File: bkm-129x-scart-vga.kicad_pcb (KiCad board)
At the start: 2 copper layers, 105 x 160 mm, 64 parts, among them J1 DB15_Female_HighDensity_Mount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, J2 SCART-F, J3 SJ1-353XNG, J5 Conn_02x32_Row_Letter_Last, J6 ICSP, Q1 DTC144EKA, Q2 MMBT3904, SW1 PBH4UEENAGX, SW2 PBH4UEENAGX, U1 ADG1611, U2 THS7374, U3 arduino-nano-v3, U4 74LVC125, U5 MIC3490-3.3, U6 ATMEGA328PB-AU, Y1 CSTNE16M0VH3L000R0

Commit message: Rev. C. Move to Kicad 5
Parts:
- moved R16 14.6 mm to (56.4, 48.5)
- moved D2 11.5 mm to (51.6, 48.5)
- moved SW1 6.59 mm to (62.3, 41.4)
- moved Q2 3.56 mm to (69.8, 32.0)
- moved R14 3.56 mm to (62.7, 35.0)
- moved R3 3.56 mm to (69.5, 34.9)
- moved R4 3.56 mm to (75.3, 32.9)
- moved R5 3.56 mm to (78.3, 32.9)
- moved R15 3.53 mm to (56.2, 34.4)
- moved R2 1.75 mm to (62.7, 31.9)
- moved D1 0.76 mm to (51.5, 34.4)
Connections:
- U2 pad 9: GND -> +3V3
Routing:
- net VDD: track 174.7 -> 196.2 mm
- net /HV_SYNC_ACT: track 14.6 -> 6.57 mm
- net /CSYNC_ACT: track 17.6 -> 10.2 mm, vias 0 -> 1
- net /H_SYNC: track 37.7 -> 31.2 mm
- net Net-(D1-Pad1): track 6.19 -> 2.31 mm
- net Net-(D2-Pad1): track 6.10 -> 2.43 mm
- net /COMB_V_SYNC: track 8.41 -> 11.6 mm
- net /COMB_CSYNC: track 12.6 -> 15.5 mm
- net /COMB_H_SYNC: track 5.87 -> 8.17 mm
- net /CSYNC: track 56.1 -> 58.0 mm
- net Net-(Q2-Pad3): track 6.00 -> 4.21 mm
- net Net-(R14-Pad2): track 5.42 -> 6.87 mm
- net /V_SYNC: track 28.5 -> 27.1 mm
- net GND: track 13.0 -> 11.7 mm, vias 10 -> 9
- net +3V3: track 16.0 -> 16.7 mm
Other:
- rule pad_to_mask_clearance: 0.2 -> 0
- board text added: "Rev. C"
- board text removed: "Rev. B"

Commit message: Rev. D
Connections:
- J1 pad 9: GND -> (no net)
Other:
- board text added: "Rev. D"
- board text removed: "Rev. C"

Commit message: Correct U5 part number
Schematic says it's the -3.3 version.
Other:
- board text added: "U1 - ADG1611 U2 - THS7374 U3 - Arduino Nano v3 (5V/16MHz) U4 - 74VHC125 U5 - MIC3490-3.3 Q1 - DTC144EKA Q2 - MMBT3904 D1 - YELLOW 0805 LED D2 - RED 0805 LED U1/2/4: TSSOP14 SW1/SW2: PBH4UEEN J3: CUI SJ1-353XNG (Like SJ1-3533NG)"
- board text removed: "U1 - ADG1611 U2 - THS7374 U3 - Arduino Nano v3 (5V/16MHz) U4 - 74VHC125 U5 - MIC3490-5.0 Q1 - DTC144EKA Q2 - MMBT3904 D1 - YELLOW 0805 LED D2 - RED 0805 LED U1/2/4: TSSOP14 SW1/SW2: PBH4UEEN J3: CUI SJ1-353XNG (Like SJ1-3533NG)"
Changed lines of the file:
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@@
     (effects (font (size 1.3 1.3) (thickness 0.25)) (justify left))
   )
-  (gr_text "U1 - ADG1611\nU2 - THS7374\nU3 - Arduino Nano v3\n      (5V/16MHz)\nU4 - 74VHC125\nU5 - MIC3490-5.0\nQ1 - DTC144EKA\nQ2 - MMBT3904\nD1 - YELLOW 0805 LED\nD2 - RED 0805 LED\nU1/2/4: TSSOP14\nSW1/SW2: PBH4UEEN\nJ3: CUI SJ1-353XNG\n(Like SJ1-3533NG)" (at 86.868 45.085) (layer F.SilkS)
+  (gr_text "U1 - ADG1611\nU2 - THS7374\nU3 - Arduino Nano v3\n      (5V/16MHz)\nU4 - 74VHC125\nU5 - MIC3490-3.3\nQ1 - DTC144EKA\nQ2 - MMBT3904\nD1 - YELLOW 0805 LED\nD2 - RED 0805 LED\nU1/2/4: TSSOP14\nSW1/SW2: PBH4UEEN\nJ3: CUI SJ1-353XNG\n(Like SJ1-3533NG)" (at 86.868 45.085) (layer F.SilkS)
     (effects (font (size 1.3 1.3) (thickness 0.25)) (justify left))
   )

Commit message: Rev. D1
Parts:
- U5: value MIC3490-3.3 -> MIC3490-5.0
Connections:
- J1 pad 5: (no net) -> GND
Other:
- board text added: "Rev. D1"
- board text added: "U1 - ADG1611 U2 - THS7374 U3 - Arduino Nano v3 (5V/16MHz) U4 - 74VHC125 U5 - MIC3490-5.0 Q1 - DTC144EKA Q2 - MMBT3904 D1 - YELLOW 0805 LED D2 - RED 0805 LED U1/2/4: TSSOP14 SW1/SW2: PBH4UEEN J3: CUI SJ1-353XNG (Like SJ1-3533NG)"
- board text removed: "Rev. D"
- board text removed: "U1 - ADG1611 U2 - THS7374 U3 - Arduino Nano v3 (5V/16MHz) U4 - 74VHC125 U5 - MIC3490-3.3 Q1 - DTC144EKA Q2 - MMBT3904 D1 - YELLOW 0805 LED D2 - RED 0805 LED U1/2/4: TSSOP14 SW1/SW2: PBH4UEEN J3: CUI SJ1-353XNG (Like SJ1-3533NG)"

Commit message: Fix R9 value on silkscreen
Schematic says R9 is 0Ω, silkscreen says it's 150Ω. Also condense the
remaining 150Ω resistors into one line.
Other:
- board text added: "R1,3,14,18 - 10K R4 - 470R R6,7,8,32,33,34 - 150R R9 - 0R (or jumper) R10,11,12,13 - 75R R19,23 - 4K7 R20,22,25,27 - 100K R2,21,24,26,28 - 100R R5,15,16 - 1K All 0805 size / 1%"
- board text removed: "R1,3,14,18 - 10K R4 - 470R R6,7,8,9 - 150R R32,33,34 - 150R R10,11,12,13 - 75R R19,23 - 4K7 R20,22,25,27 - 100K R2,21,24,26,28 - 100R R5,15,16 - 1K All 0805 size / 1%"
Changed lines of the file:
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@@
     (effects (font (size 1.3 1.3) (thickness 0.25)) (justify left))
   )
-  (gr_text "R1,3,14,18 - 10K\nR4 - 470R\nR6,7,8,9 - 150R\nR32,33,34 - 150R\nR10,11,12,13 - 75R\nR19,23 - 4K7\nR20,22,25,27 - 100K\nR2,21,24,26,28 - 100R\nR5,15,16 - 1K\nAll 0805 size / 1%" (at 128.8906 40.74) (layer F.SilkS)
+  (gr_text "R1,3,14,18 - 10K\nR4 - 470R\nR6,7,8,32,33,34 - 150R\nR9 - 0R (or jumper)\nR10,11,12,13 - 75R\nR19,23 - 4K7\nR20,22,25,27 - 100K\nR2,21,24,26,28 - 100R\nR5,15,16 - 1K\nAll 0805 size / 1%" (at 128.8906 40.74) (layer F.SilkS)
     (effects (font (size 1.3 1.3) (thickness 0.25)) (justify left))
   )

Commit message: Rev. E
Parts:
- J5: footprint din-41612-64p-ra:DIN-41612-64P -> standard-pin-64p-ra:STANDARD-PIN-64P-RA
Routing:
- net GND: vias 9 -> 10
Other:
- board text added: "Rev. E"
- board text removed: "Rev. D1"

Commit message: Update to rev. F
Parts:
- added C101: 1uF, Capacitor_SMD:C_0805_2012Metric_Pad1.18x1.45mm_HandSolder, F.Cu at (103.3, 98.2)
- added C102: 4.7uF, Capacitor_SMD:C_0805_2012Metric_Pad1.18x1.45mm_HandSolder, F.Cu at (112.0, 93.5)
- added U101: LD1117S50TR_SOT223, Package_TO_SOT_SMD:SOT-223-3_TabPin2, F.Cu at (106.5, 92.5)
- C1, C10, C11, C12, C15, C16, C17, C2, C3, C4, C5, C6, C9: footprint Capacitors_SMD:C_0805_HandSoldering -> Capacitor_SMD:C_0805_2012Metric_Pad1.18x1.45mm_HandSolder
- C13, C7, C8: footprint Capacitors_SMD:CP_Elec_6.3x5.3 -> Capacitor_SMD:CP_Elec_6.3x5.3
- D1, D2: footprint Diodes_SMD:D_0805 -> Diode_SMD:D_0805_2012Metric_Pad1.15x1.40mm_HandSolder
- Q1: footprint TO_SOT_Packages_SMD:SC-59_Handsoldering -> Package_TO_SOT_SMD:SC-59_Handsoldering
- Q2: footprint TO_SOT_Packages_SMD:SOT-23_Handsoldering -> Package_TO_SOT_SMD:SOT-23_Handsoldering
- R1, R10, R11, R12, R13, R14, R15, R16, R18, R19, R2, R20, R21, R22, R23, R24, R25, R26, R27, R28, R3, R32, R33, R34, R4, R5, R6, R7, R8, R9: footprint Resistors_SMD:R_0805_HandSoldering -> Resistor_SMD:R_0805_2012Metric_Pad1.20x1.40mm_HandSolder
- U1: footprint Housings_SSOP:TSSOP-16_4.4x5mm_Pitch0.65mm -> Package_SO:TSSOP-16_4.4x5mm_P0.65mm
- U2, U4: footprint Housings_SSOP:TSSOP-14_4.4x5mm_Pitch0.65mm -> Package_SO:TSSOP-14_4.4x5mm_P0.65mm
- U5: footprint TO_SOT_Packages_SMD:SOT-23-5_HandSoldering -> Package_TO_SOT_SMD:SOT-23-5_HandSoldering
- U6: footprint Housings_QFP:TQFP-32_7x7mm_Pitch0.8mm -> Package_QFP:TQFP-32_7x7mm_P0.8mm
- Y1: footprint muRata-CSTNEx:CSTNEx -> Crystal:Resonator_SMD_muRata_CSTxExxV-3Pin_3.0x1.1mm
- moved C6 0.19 mm to (116.1, 96.1)
- moved C9 0.19 mm to (132.8, 96.1)
- moved C17 0.13 mm to (98.9, 145.4)
- moved Y1 0.09 mm to (111.5, 135.1)
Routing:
- net +3V3: track 16.7 -> 45.6 mm
- net /OUT_G: track 25.5 -> 21.7 mm
- net VDD: track 196.2 -> 199.5 mm
- net +5VD: track 138.6 -> 135.6 mm
- net ~EXT_SYNC_OE: track 46.0 -> 43.4 mm
- net GND: track 11.7 -> 13.7 mm, vias 10 -> 14
- net ~MCU_RESET: track 35.9 -> 36.4 mm
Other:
- board text added: "C7,8,13 - 100uF/16V 6,3x5,3mm Electrolytical C10 - 2.2uF or C102 - 4.7uF C11 - 1.0uF or C101 - 1.0uF Rest - 0.1uF 25V / 0805"
- board text added: "Only mount one of these sections"
- board text added: "Rev. F"
- board text added: "U1 - ADG1611BRUZ or DG1411EEQ U2 - THS7374 U3 - Arduino Nano v3 (5V/16MHz) U4 - 74VHC125 U5 - MIC3490-5.0 or U101 - LD1117S50TR Q1 - DTC144EKA Q2 - MMBT3904 D1 - YELLOW 0805 LED D2 - RED 0805 LED U1/2/4: TSSOP14 SW1/SW2: PBH4UEEN J3: CUI SJ1-353XNG (Like SJ1-3533NG)"
- board text removed: "C7,8,13 - 100uF/16V 6,3x5,3mm Electrolytical C10 - 2.2uF C11 - 1.0uF Rest - 0.1uF 25V / 0805"
- board text removed: "Rev. E"
- board text removed: "U1 - ADG1611 U2 - THS7374 U3 - Arduino Nano v3 (5V/16MHz) U4 - 74VHC125 U5 - MIC3490-5.0 Q1 - DTC144EKA Q2 - MMBT3904 D1 - YELLOW 0805 LED D2 - RED 0805 LED U1/2/4: TSSOP14 SW1/SW2: PBH4UEEN J3: CUI SJ1-353XNG (Like SJ1-3533NG)"

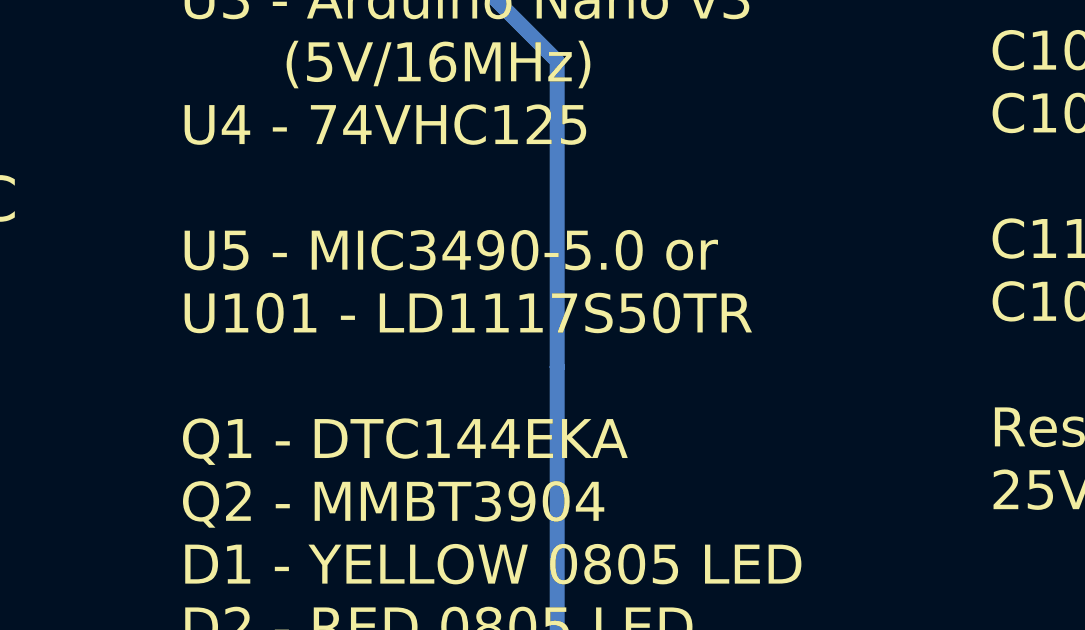
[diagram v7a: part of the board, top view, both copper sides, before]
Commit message: Fixed 1117 PN to LDL1117S50R
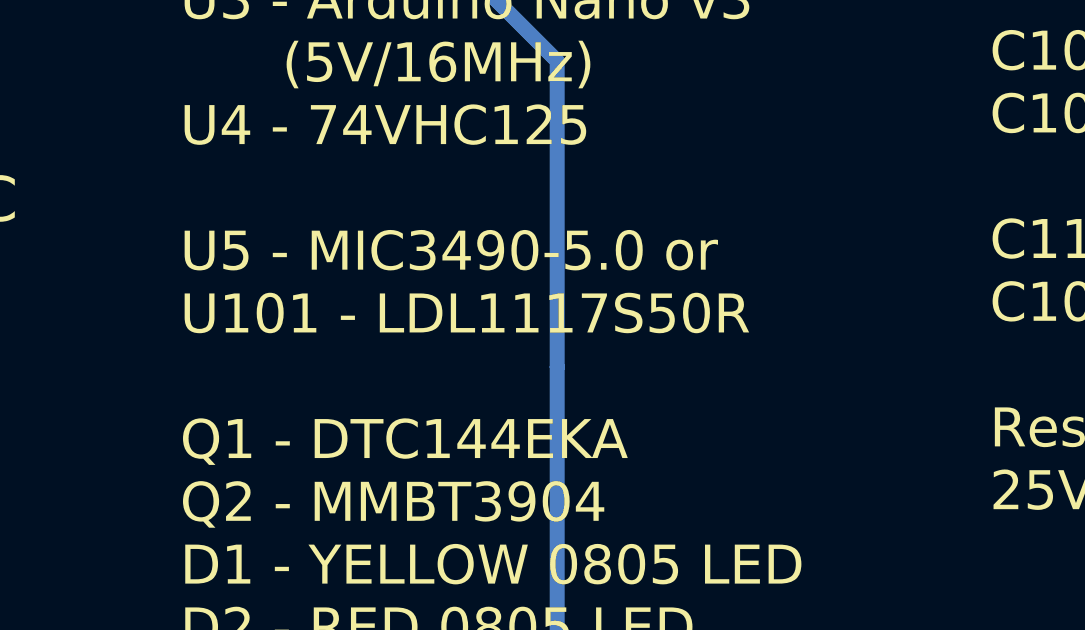
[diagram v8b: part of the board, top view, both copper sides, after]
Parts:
- U101: value LD1117S50TR_SOT223 -> LDL1117S50R
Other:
- board text added: "U1 - ADG1611BRUZ or DG1411EEQ U2 - THS7374 U3 - Arduino Nano v3 (5V/16MHz) U4 - 74VHC125 U5 - MIC3490-5.0 or U101 - LDL1117S50R Q1 - DTC144EKA Q2 - MMBT3904 D1 - YELLOW 0805 LED D2 - RED 0805 LED U1/2/4: TSSOP14 SW1/SW2: PBH4UEEN J3: CUI SJ1-353XNG (Like SJ1-3533NG)"
- board text removed: "U1 - ADG1611BRUZ or DG1411EEQ U2 - THS7374 U3 - Arduino Nano v3 (5V/16MHz) U4 - 74VHC125 U5 - MIC3490-5.0 or U101 - LD1117S50TR Q1 - DTC144EKA Q2 - MMBT3904 D1 - YELLOW 0805 LED D2 - RED 0805 LED U1/2/4: TSSOP14 SW1/SW2: PBH4UEEN J3: CUI SJ1-353XNG (Like SJ1-3533NG)"
